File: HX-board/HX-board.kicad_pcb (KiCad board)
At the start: 2 copper layers, 63.5 x 63.5 mm, 61 parts, among them J1 Testpoints, J2 PCIE-LP-01-01-F-DV-A-TR, J3 DB15_Female, J4 Testpoints, J5 DB15_Female, Q1 MMBT4403LT3G, Q2 MMBT4403LT3G, Q3 MMBT4403LT3G, Q4 MMBT4403LT3G, Q5 MMBT4403LT3G, Q6 MMBT4403LT3G, Q7 MMBT4403LT3G, U1 HX711, U2 HX711, U3 HX711, U4 HX711, U5 HX711, U6 HX711, U7 HX711

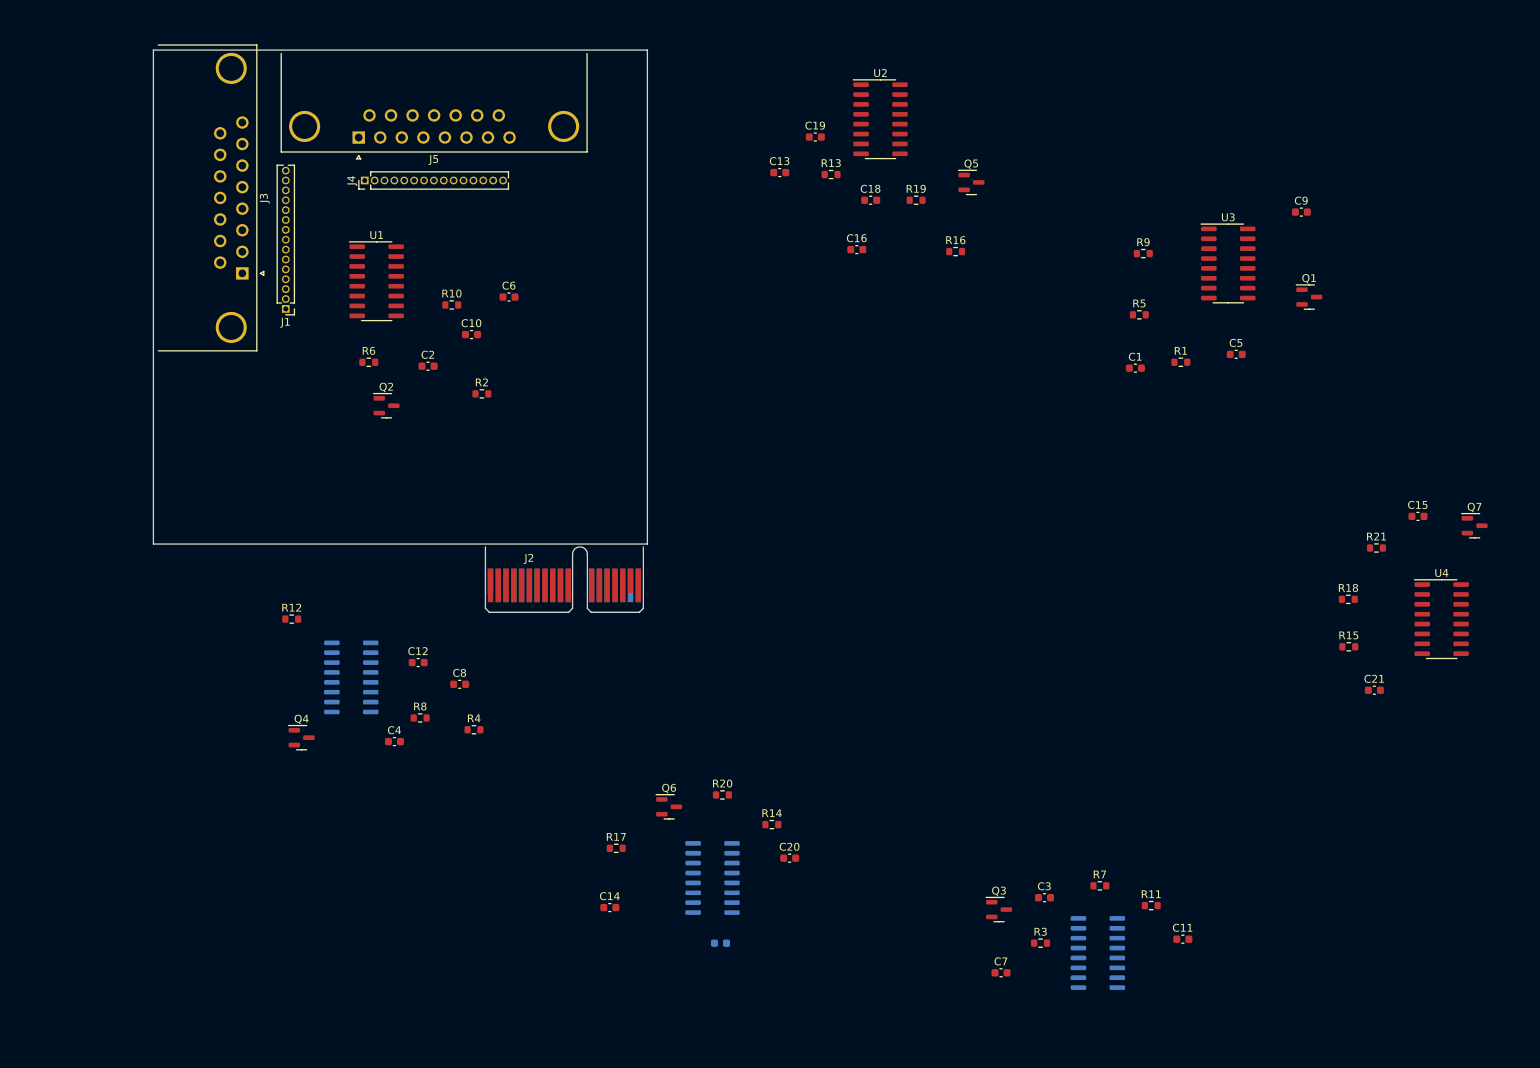
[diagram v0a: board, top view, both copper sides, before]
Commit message: Updated pcie and fixed HX, MOSFET, TC board. Also added hierarchical sheet.
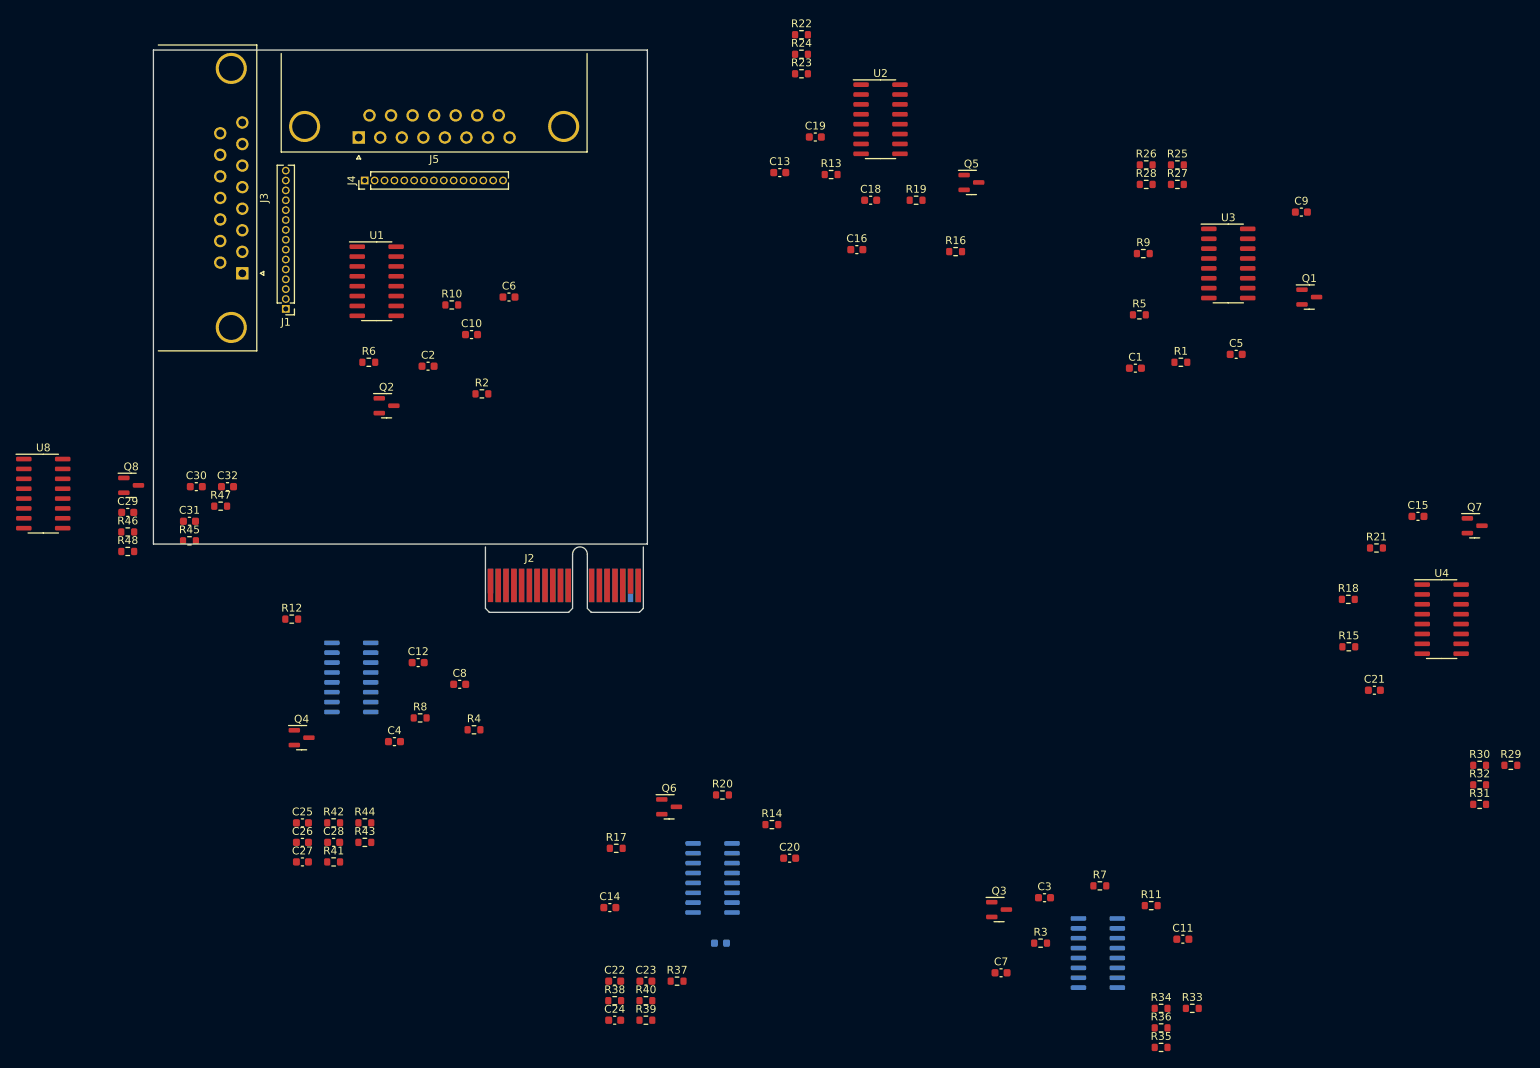
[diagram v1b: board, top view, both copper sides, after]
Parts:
- added C22: 10uF, Capacitor_SMD:C_0603_1608Metric, F.Cu at (160.9, 183.2)
- added C23: 0.1uF, Capacitor_SMD:C_0603_1608Metric, F.Cu at (164.9, 183.2)
- added C24: 0.1uF, Capacitor_SMD:C_0603_1608Metric, F.Cu at (160.9, 188.2)
- added C25: 10uF, Capacitor_SMD:C_0603_1608Metric, F.Cu at (120.8, 162.8)
- added C26: 10uF, Capacitor_SMD:C_0603_1608Metric, F.Cu at (120.8, 165.4)
- added C27: 0.1uF, Capacitor_SMD:C_0603_1608Metric, F.Cu at (120.8, 167.9)
- added C28: 0.1uF, Capacitor_SMD:C_0603_1608Metric, F.Cu at (124.8, 165.4)
- added C29: 10uF, Capacitor_SMD:C_0603_1608Metric, F.Cu at (98.3, 122.9)
- added C30: 10uF, Capacitor_SMD:C_0603_1608Metric, F.Cu at (107.1, 119.6)
- added C31: 0.1uF, Capacitor_SMD:C_0603_1608Metric, F.Cu at (106.2, 124.1)
- added C32: 0.1uF, Capacitor_SMD:C_0603_1608Metric, F.Cu at (111.1, 119.6)
- added Q8: MMBT4403LT3G, Package_TO_SOT_SMD:SOT-23, F.Cu at (98.7, 119.5)
- added R22: 8.2kΩ, Resistor_SMD:R_0603_1608Metric, F.Cu at (184.9, 61.5)
- added R23: 100Ω, Resistor_SMD:R_0603_1608Metric, F.Cu at (184.9, 66.5)
- added R24: 100Ω, Resistor_SMD:R_0603_1608Metric, F.Cu at (184.9, 64.0)
- added R25: 20kΩ, Resistor_SMD:R_0603_1608Metric, F.Cu at (233.2, 78.3)
- added R26: 8.2kΩ, Resistor_SMD:R_0603_1608Metric, F.Cu at (229.2, 78.3)
- added R27: 100Ω, Resistor_SMD:R_0603_1608Metric, F.Cu at (233.2, 80.8)
- added R28: 100Ω, Resistor_SMD:R_0603_1608Metric, F.Cu at (229.2, 80.8)
- added R29: 20kΩ, Resistor_SMD:R_0603_1608Metric, F.Cu at (276.1, 155.4)
- added R30: 8.2kΩ, Resistor_SMD:R_0603_1608Metric, F.Cu at (272.1, 155.4)
- added R31: 100Ω, Resistor_SMD:R_0603_1608Metric, F.Cu at (272.1, 160.5)
- added R32: 100Ω, Resistor_SMD:R_0603_1608Metric, F.Cu at (272.1, 158.0)
- added R33: 20kΩ, Resistor_SMD:R_0603_1608Metric, F.Cu at (235.2, 186.7)
- added R34: 8.2kΩ, Resistor_SMD:R_0603_1608Metric, F.Cu at (231.1, 186.7)
- added R35: 100Ω, Resistor_SMD:R_0603_1608Metric, F.Cu at (231.1, 191.7)
- added R36: 100Ω, Resistor_SMD:R_0603_1608Metric, F.Cu at (231.1, 189.2)
- added R37: 20kΩ, Resistor_SMD:R_0603_1608Metric, F.Cu at (168.9, 183.2)
- added R38: 8.2kΩ, Resistor_SMD:R_0603_1608Metric, F.Cu at (160.9, 185.7)
- added R39: 100Ω, Resistor_SMD:R_0603_1608Metric, F.Cu at (164.9, 188.2)
- added R40: 100Ω, Resistor_SMD:R_0603_1608Metric, F.Cu at (164.9, 185.7)
- added R41: 20kΩ, Resistor_SMD:R_0603_1608Metric, F.Cu at (124.8, 167.9)
- added R42: 8.2kΩ, Resistor_SMD:R_0603_1608Metric, F.Cu at (124.8, 162.8)
- added R43: 100Ω, Resistor_SMD:R_0603_1608Metric, F.Cu at (128.8, 165.4)
- added R44: 100Ω, Resistor_SMD:R_0603_1608Metric, F.Cu at (128.8, 162.8)
- added R45: 20kΩ, Resistor_SMD:R_0603_1608Metric, F.Cu at (106.2, 126.6)
- added R46: 8.2kΩ, Resistor_SMD:R_0603_1608Metric, F.Cu at (98.3, 125.4)
- added R47: 100Ω, Resistor_SMD:R_0603_1608Metric, F.Cu at (110.2, 122.1)
- added R48: 100Ω, Resistor_SMD:R_0603_1608Metric, F.Cu at (98.3, 128.0)
- added U8: HX711, Package_SO:SOP-16_3.9x9.9mm_P1.27mm, F.Cu at (87.4, 120.5)
- C10, C21, C9: value 0.1uF -> 10uF
- C15, C16, C3, C4, C7, C8: value 10uF -> 0.1uF
- R1, R13, R14, R2, R3: value 20kΩ -> 2kΩ
- R10, R11, R12: value 100Ω -> 100kΩ
- R15, R4: value 20kΩ -> 100kΩ
- R16, R5, R6: value 8.2kΩ -> 100kΩ
- R17: value 8.2kΩ -> 20kΩ
- R21: value 100Ω -> 20kΩ
- R7, R8: value 8.2kΩ -> 2kΩ
- R9: value 100Ω -> 2kΩ
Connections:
- C10 pad 2: Net-(C10-Pad2) -> /HX3_E+
- C11 pad 2: Net-(C11-Pad2) -> Net-(U3-Pad6)
- C12 pad 1: GND -> Net-(U3-Pad7)
- C12 pad 2: Net-(C12-Pad2) -> Net-(U3-Pad8)
- C14 pad 2: +5V -> /HX4_E+
- C15 pad 2: +5V -> Net-(U4-Pad6)
- C16 pad 1: GND -> Net-(U4-Pad7)
- C16 pad 2: /HX2_E+ -> Net-(U4-Pad8)
- C17 pad 2: /HX6_E+ -> +5V
- C18 pad 2: /HX4_E+ -> /HX5_E+
- C19 pad 2: Net-(C19-Pad2) -> Net-(U5-Pad6)
- C2 pad 2: +5V -> /HX1_E+
- C20 pad 1: GND -> Net-(U5-Pad7)
- C20 pad 2: Net-(C20-Pad2) -> Net-(U5-Pad8)
- C21 pad 2: Net-(C21-Pad2) -> +5V
- C3 pad 2: +5V -> Net-(U1-Pad6)
- C4 pad 1: GND -> Net-(U1-Pad7)
- C4 pad 2: +5V -> Net-(U1-Pad8)
- C5 pad 2: /HX3_E+ -> +5V
- C6 pad 2: /HX1_E+ -> /HX2_E+
- C7 pad 2: /HX5_E+ -> Net-(U2-Pad6)
- C8 pad 1: GND -> Net-(U2-Pad7)
- C8 pad 2: /HX7_E+ -> Net-(U2-Pad8)
- C9 pad 2: Net-(C9-Pad2) -> +5V
- J1 pad 11: /HX3_A -> /HX3_A+
- J1 pad 15: /HX4_A -> /HX4_A+
- J1 pad 3: /HX1_A -> /HX1_A+
- J1 pad 7: /HX2_A -> /HX2_A+
- J2 pad A7: /HX5_DT -> /HX6_DT
- J2 pad A8: /HX6_DT -> /HX7_DT
- J2 pad A9: /HX7_DT -> /HX8_DT
- J2 pad B13: unconnected-(J2-PadB13) -> +3.3V
- J2 pad B14: unconnected-(J2-PadB14) -> +3.3V
- J2 pad B8: GND -> /HX5_DT
- J3 pad 2: /HX1_A -> /HX1_A+
- J3 pad 4: /HX2_A -> /HX2_A+
- J3 pad 6: /HX3_A -> /HX3_A+
- J3 pad 8: /HX4_A -> /HX4_A+
- J4 pad 11: /HX7_A -> /HX7_A+
- J4 pad 13: unconnected-(J4-Pad13) -> /HX8_E+
- J4 pad 14: unconnected-(J4-Pad14) -> GND
- J4 pad 15: unconnected-(J4-Pad15) -> /HX8_A+
- J4 pad 3: /HX5_A -> /HX5_A+
- J4 pad 7: /HX6_A -> /HX6_A+
- J5 pad 15: unconnected-(J5-Pad15) -> GND
- J5 pad 2: /HX5_A -> /HX5_A+
- J5 pad 4: /HX6_A -> /HX6_A+
- J5 pad 6: /HX7_A -> /HX7_A+
- J5 pad 7: unconnected-(J5-Pad7) -> /HX8_E+
- J5 pad 8: unconnected-(J5-Pad8) -> /HX8_A+
- Q1 pad 1: Net-(Q1-Pad1) -> Net-(U1-Pad2)
- Q1 pad 3: /HX3_E+ -> /HX1_E+
- Q2 pad 1: Net-(Q2-Pad1) -> Net-(U2-Pad2)
- Q2 pad 3: /HX1_E+ -> /HX2_E+
- Q3 pad 1: Net-(Q3-Pad1) -> Net-(U3-Pad2)
- Q3 pad 3: /HX5_E+ -> /HX3_E+
- Q4 pad 1: Net-(Q4-Pad1) -> Net-(U4-Pad2)
- Q4 pad 3: /HX7_E+ -> /HX4_E+
- Q5 pad 1: Net-(Q5-Pad1) -> Net-(U5-Pad2)
- Q5 pad 3: /HX2_E+ -> /HX5_E+
- Q7 pad 1: Net-(Q7-Pad1) -> Net-(U7-Pad2)
- Q7 pad 3: /HX4_E+ -> /HX7_E+
- R1 pad 1: Net-(R1-Pad1) -> GND
- R1 pad 2: /HX3_E+ -> /HX711 3/A+
- R10 pad 1: Net-(U1-Pad7) -> /HX4_A+
- R10 pad 2: /HX1_A -> /HX711 4/A+
- R11 pad 1: Net-(R11-Pad1) -> /HX6_A+
- R11 pad 2: /HX5_A -> /HX711 6/A+
- R12 pad 1: Net-(R12-Pad1) -> /HX5_A+
- R12 pad 2: /HX7_A -> /HX711 5/A+
- R13 pad 1: Net-(R13-Pad1) -> GND
- R13 pad 2: /HX2_E+ -> /HX711 7/A+
- R14 pad 1: Net-(R14-Pad1) -> GND
- R14 pad 2: /HX6_E+ -> /HX711 8/A+
- R15 pad 1: Net-(R15-Pad1) -> /HX7_A+
- R15 pad 2: /HX4_E+ -> /HX711 7/A+
- R16 pad 1: GND -> /HX8_A+
- R16 pad 2: Net-(R13-Pad1) -> /HX711 8/A+
- R17 pad 1: GND -> Net-(U1-Pad4)
- R17 pad 2: Net-(R14-Pad1) -> /HX1_E+
- R18 pad 2: Net-(R15-Pad1) -> Net-(U1-Pad4)
- R19 pad 1: Net-(R19-Pad1) -> Net-(U1-Pad8)
- R19 pad 2: /HX2_A -> /HX711 1/A+
- R2 pad 1: Net-(R2-Pad1) -> GND
- R2 pad 2: /HX1_E+ -> /HX711 2/A+
- R20 pad 1: Net-(R20-Pad1) -> Net-(U1-Pad7)
- R20 pad 2: /HX6_A -> GND
- R21 pad 1: Net-(R21-Pad1) -> Net-(U2-Pad4)
- R21 pad 2: /HX4_A -> /HX2_E+
- R3 pad 1: Net-(R3-Pad1) -> GND
- R3 pad 2: /HX5_E+ -> /HX711 1/A+
- R4 pad 1: Net-(R4-Pad1) -> /HX3_A+
- R4 pad 2: /HX7_E+ -> /HX711 3/A+
- R5 pad 1: GND -> /HX2_A+
- R5 pad 2: Net-(R1-Pad1) -> /HX711 2/A+
- R6 pad 1: GND -> /HX1_A+
- R6 pad 2: Net-(R2-Pad1) -> /HX711 1/A+
- R7 pad 2: Net-(R3-Pad1) -> /HX711 4/A+
- R8 pad 2: Net-(R4-Pad1) -> /HX711 6/A+
- R9 pad 1: Net-(U3-Pad7) -> GND
- R9 pad 2: /HX3_A -> /HX711 5/A+
- U1 pad 16: +5V -> +3.3V
- U1 pad 2: Net-(Q2-Pad1) -> Net-(U1-Pad2)
- U1 pad 4: Net-(R2-Pad1) -> Net-(U1-Pad4)
- U1 pad 6: Net-(C10-Pad2) -> Net-(U1-Pad6)
- U1 pad 8: Net-(U1-Pad7) -> Net-(U1-Pad8)
- U2 pad 16: +5V -> +3.3V
- U2 pad 2: Net-(Q5-Pad1) -> Net-(U2-Pad2)
- U2 pad 4: Net-(R13-Pad1) -> Net-(U2-Pad4)
- U2 pad 6: Net-(C19-Pad2) -> Net-(U2-Pad6)
- U2 pad 7: Net-(R19-Pad1) -> Net-(U2-Pad7)
- U2 pad 8: Net-(R19-Pad1) -> Net-(U2-Pad8)
- U3 pad 16: +5V -> +3.3V
- U3 pad 2: Net-(Q1-Pad1) -> Net-(U3-Pad2)
- U3 pad 4: Net-(R1-Pad1) -> Net-(U3-Pad4)
- U3 pad 6: Net-(C9-Pad2) -> Net-(U3-Pad6)
- U3 pad 8: Net-(U3-Pad7) -> Net-(U3-Pad8)
- U4 pad 16: +5V -> +3.3V
- U4 pad 2: Net-(Q7-Pad1) -> Net-(U4-Pad2)
- U4 pad 4: Net-(R15-Pad1) -> Net-(U4-Pad4)
- U4 pad 6: Net-(C21-Pad2) -> Net-(U4-Pad6)
- U4 pad 7: Net-(R21-Pad1) -> Net-(U4-Pad7)
- U4 pad 8: Net-(R21-Pad1) -> Net-(U4-Pad8)
- U5 pad 16: +5V -> +3.3V
- U5 pad 2: Net-(Q3-Pad1) -> Net-(U5-Pad2)
- U5 pad 4: Net-(R3-Pad1) -> Net-(U5-Pad4)
- U5 pad 6: Net-(C11-Pad2) -> Net-(U5-Pad6)
- U5 pad 7: Net-(R11-Pad1) -> Net-(U5-Pad7)
- U5 pad 8: Net-(R11-Pad1) -> Net-(U5-Pad8)
- U6 pad 16: +5V -> +3.3V
- U6 pad 4: Net-(R14-Pad1) -> Net-(U6-Pad4)
- U6 pad 6: Net-(C20-Pad2) -> Net-(U6-Pad6)
- U6 pad 7: Net-(R20-Pad1) -> Net-(U6-Pad7)
- U6 pad 8: Net-(R20-Pad1) -> Net-(U6-Pad8)
- U7 pad 16: +5V -> +3.3V
- U7 pad 2: Net-(Q4-Pad1) -> Net-(U7-Pad2)
- U7 pad 4: Net-(R4-Pad1) -> Net-(U7-Pad4)
- U7 pad 6: Net-(C12-Pad2) -> Net-(U7-Pad6)
- U7 pad 7: Net-(R12-Pad1) -> Net-(U7-Pad7)
- U7 pad 8: Net-(R12-Pad1) -> Net-(U7-Pad8)

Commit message: updates for layout MOSFET/HX
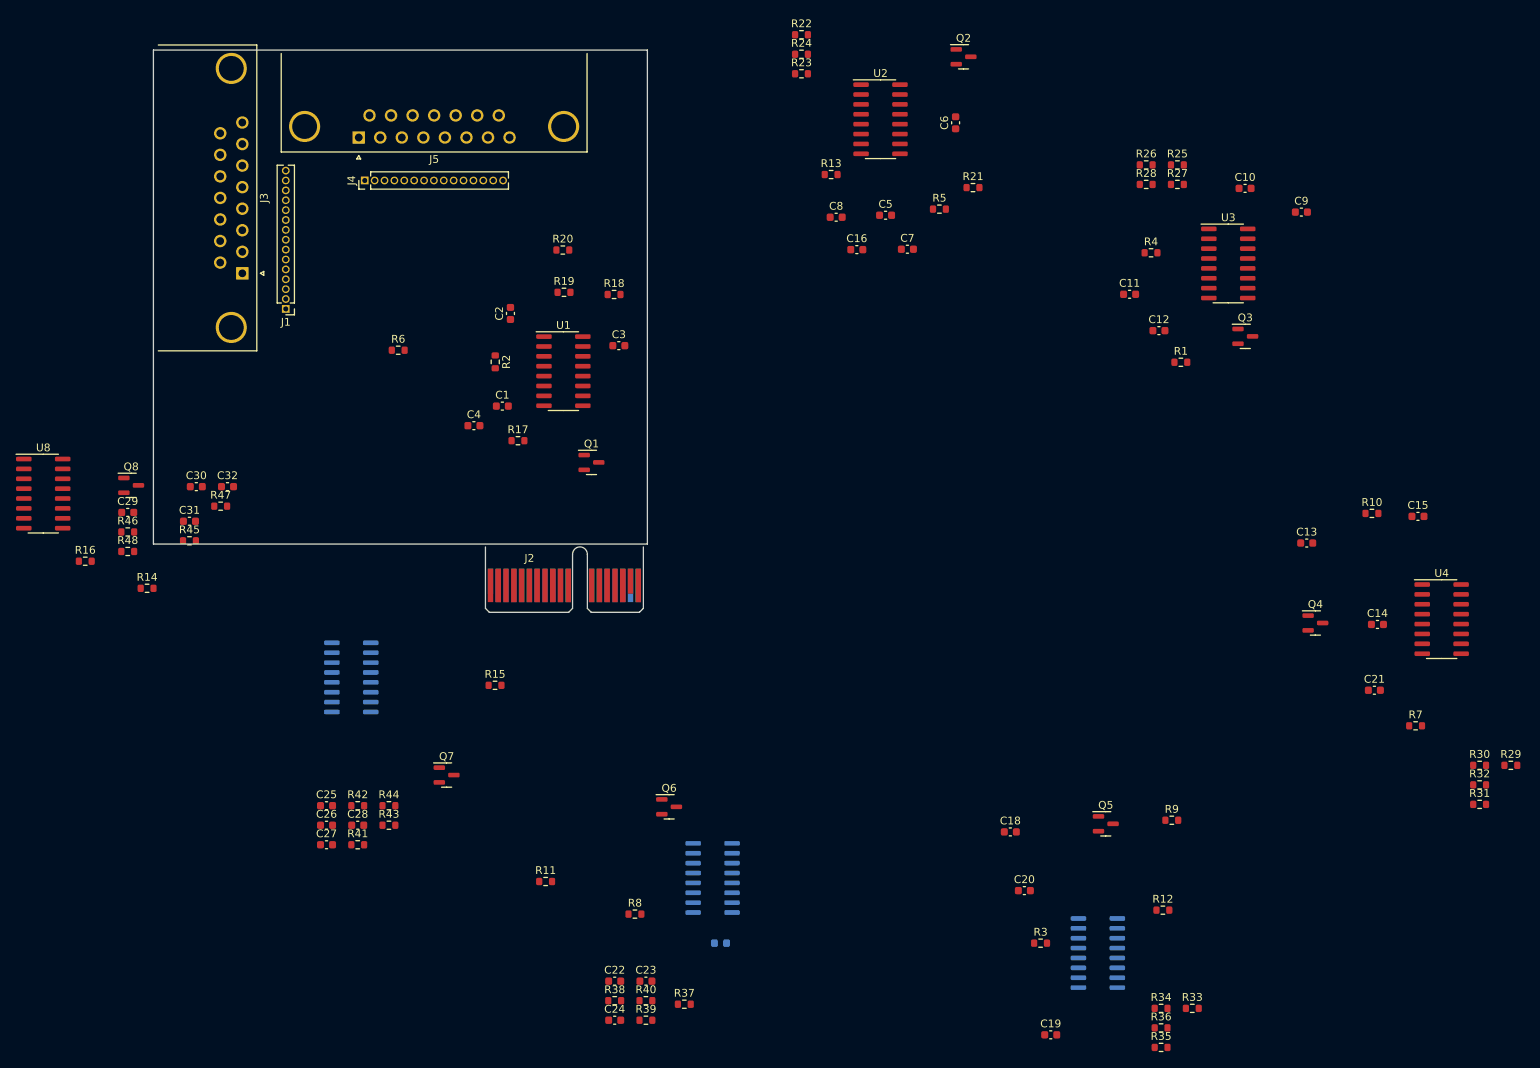
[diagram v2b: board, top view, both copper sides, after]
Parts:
- moved Q7 136.0 mm to (139.3, 156.7)
- moved Q4 131.2 mm to (251.0, 137.1)
- moved R10 121.3 mm to (258.2, 123.1)
- moved C19 119.3 mm to (217.0, 190.1)
- moved R16 118.8 mm to (92.8, 129.2)
- moved R12 118.1 mm to (231.4, 174.1)
- moved R15 109.9 mm to (145.5, 145.2)
- moved R4 106.5 mm to (229.8, 89.6)
- moved C14 105.2 mm to (259.0, 137.3)
- moved C12 104.3 mm to (230.9, 99.6)
- moved R18 102.2 mm to (160.8, 94.9)
- moved C10 101.2 mm to (241.9, 81.3)
- moved Q1 94.7 mm to (157.9, 116.5)
- moved C7 93.8 mm to (198.5, 89.1)
- moved C3 89.6 mm to (161.4, 101.5)
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
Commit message: Revert "Revert "HX and TC Board mostly finished""
This reverts commit 2ae13608b6027366e1c59111a8dca91d16e06deb.
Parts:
- C18, C19, C20, C22, C23, C24, C25, C26, C27, C28, Q5, Q6, Q7, R11, R12, R15, R3, R33, R34, R35, R36, R37, R38, R39, R40, R41, R42, R43, R44, R8, R9: moved to B.Cu
- moved R7 152.9 mm to (123.2, 90.4)
- moved R10 140.9 mm to (124.0, 80.5)
- moved R29 139.6 mm to (152.9, 89.9), turned to 90 degrees
- moved R30 138.9 mm to (148.6, 91.9), turned to 90 degrees
- moved C9 135.3 mm to (115.6, 105.4), turned to 180 degrees
- moved Q3 131.9 mm to (110.2, 106.4), turned to 180 degrees
- moved R31 131.8 mm to (156.3, 97.5), turned to 180 degrees
- moved R25 128.2 mm to (109.2, 110.9), turned to 90 degrees
- moved R26 125.4 mm to (109.2, 114.7), turned to 90 degrees
- moved R32 124.4 mm to (163.3, 97.5)
- moved C10 124.4 mm to (119.9, 105.4), turned to 180 degrees
- moved U3 124.1 mm to (117.6, 112.9)
- moved R27 123.8 mm to (115.8, 120.1)
- moved C14 120.9 mm to (148.6, 87.9), turned to -90 degrees
- moved C12 120.9 mm to (111.8, 120.1)
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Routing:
- net GND: track 0.00 -> 697.2 mm, vias 0 -> 33
- net +5V: track 0.00 -> 273.3 mm, vias 0 -> 20
- net +3.3V: track 0.00 -> 194.6 mm, vias 0 -> 22
- net /HX_CLK: track 0.00 -> 157.9 mm, vias 0 -> 9
- net /HX1_A+: track 0.00 -> 104.5 mm, vias 0 -> 2
- net /HX1_E+: track 0.00 -> 98.3 mm, vias 0 -> 4
- net /HX4_DT: track 0.00 -> 92.0 mm, vias 0 -> 6
- net /HX7_E+: track 0.00 -> 87.2 mm, vias 0 -> 2
- net /HX6_E+: track 0.00 -> 64.8 mm, vias 0 -> 3
- net /HX5_A+: track 0.00 -> 59.8 mm, vias 0 -> 8
- net /HX5_E+: track 0.00 -> 59.5 mm, vias 0 -> 2
- net /HX4_E+: track 0.00 -> 56.5 mm, vias 0 -> 6
- net /HX2_E+: track 0.00 -> 56.0 mm, vias 0 -> 4
- net /HX711 4/A+: track 0.00 -> 54.4 mm, vias 0 -> 2
- net /HX7_DT: track 0.00 -> 53.2 mm, vias 0 -> 2
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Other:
- board size 63.5 x 63.5 mm -> 63.5 x 63.9 mm

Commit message: Revert "HX and TC Board mostly finished"
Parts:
- C18, C19, C20, C22, C23, C24, C25, C26, C27, C28, Q5, Q6, Q7, R11, R12, R15, R3, R33, R34, R35, R36, R37, R38, R39, R40, R41, R42, R43, R44, R8, R9: moved to F.Cu
- moved R7 152.9 mm to (263.9, 150.4)
- moved R10 140.9 mm to (258.2, 123.1)
- moved R29 139.6 mm to (276.1, 155.4), turned to 0 degrees
- moved R30 138.9 mm to (272.1, 155.4), turned to 0 degrees
- moved C9 135.3 mm to (249.2, 84.3), turned to 0 degrees
- moved Q3 131.9 mm to (242.0, 100.3), turned to 0 degrees
- moved R31 131.8 mm to (272.1, 160.5), turned to 0 degrees
- moved R25 128.2 mm to (233.2, 78.3), turned to 0 degrees
- moved R26 125.4 mm to (229.2, 78.3), turned to 0 degrees
- moved R32 124.4 mm to (272.1, 158.0)
- moved C10 124.4 mm to (241.9, 81.3), turned to 0 degrees
- moved U3 124.1 mm to (239.8, 90.9)
- moved R27 123.8 mm to (233.2, 80.8)
- moved C14 120.9 mm to (259.0, 137.3), turned to 0 degrees
- moved C12 120.9 mm to (230.9, 99.6)
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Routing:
- net GND: track 697.2 -> 0.00 mm, vias 33 -> 0
- net +5V: track 273.3 -> 0.00 mm, vias 20 -> 0
- net +3.3V: track 194.6 -> 0.00 mm, vias 22 -> 0
- net /HX_CLK: track 157.9 -> 0.00 mm, vias 9 -> 0
- net /HX1_A+: track 104.5 -> 0.00 mm, vias 2 -> 0
- net /HX1_E+: track 98.3 -> 0.00 mm, vias 4 -> 0
- net /HX4_DT: track 92.0 -> 0.00 mm, vias 6 -> 0
- net /HX7_E+: track 87.2 -> 0.00 mm, vias 2 -> 0
- net /HX6_E+: track 64.8 -> 0.00 mm, vias 3 -> 0
- net /HX5_A+: track 59.8 -> 0.00 mm, vias 8 -> 0
- net /HX5_E+: track 59.5 -> 0.00 mm, vias 2 -> 0
- net /HX4_E+: track 56.5 -> 0.00 mm, vias 6 -> 0
- net /HX2_E+: track 56.0 -> 0.00 mm, vias 4 -> 0
- net /HX711 4/A+: track 54.4 -> 0.00 mm, vias 2 -> 0
- net /HX7_DT: track 53.2 -> 0.00 mm, vias 2 -> 0
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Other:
- board size 63.5 x 63.9 mm -> 63.5 x 63.5 mm
